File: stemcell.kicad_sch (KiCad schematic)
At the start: 36 parts, among them J1 USB C Connector, J2 Left, J3 Right, J4 Down, SW1 Boot0, U1 STM32F4x1CxUx, U2 XC6220B331MR, Y1 HSE1 8Mhz 12pF

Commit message: updated to use type-c-31-m-12, since it's more commonly available
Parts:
- J1: footprint stemcell:USB-C-C168688 -> Connector_USB:USB_C_Receptacle_HRO_TYPE-C-31-M-12; LCSC C2681554 -> C165948
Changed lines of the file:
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@@
     (property "Reference" "J1" (id 0) (at 123.952 30.734 0))
     (property "Value" "USB C Connector" (id 1) (at 123.952 33.274 0))
-    (property "Footprint" "stemcell:USB-C-C168688" (id 2) (at 127.762 54.229 0)
+    (property "Footprint" "Connector_USB:USB_C_Receptacle_HRO_TYPE-C-31-M-12" (id 2) (at 127.762 54.229 0)
       (effects (font (size 1.27 1.27)) hide)
     )
@@
       (effects (font (size 1.27 1.27)) hide)
     )
-    (property "LCSC" "C2681554" (id 4) (at 123.952 54.229 0)
+    (property "LCSC" "C165948" (id 4) (at 123.952 54.229 0)
       (effects (font (size 1.27 1.27)) hide)
     )
@@
     )
     (path "/a4788c8d-5773-43fe-9711-99f01fa6cfd8"
-      (reference "J1") (unit 1) (value "USB C Connector") (footprint "stemcell:USB-C-C168688")
+      (reference "J1") (unit 1) (value "USB C Connector") (footprint "Connector_USB:USB_C_Receptacle_HRO_TYPE-C-31-M-12")
     )
     (path "/30cde441-a4b4-4a86-92b5-1140e5d06e66"

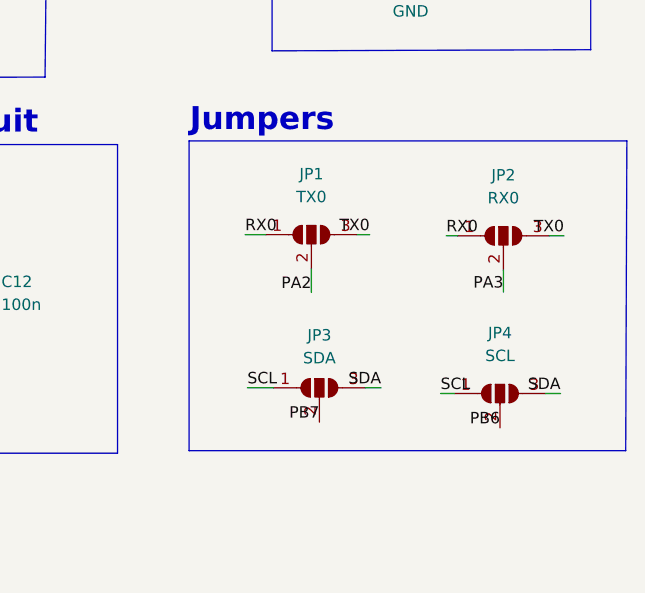
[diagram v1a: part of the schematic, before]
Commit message: added pre-soldered jumpers on the N position, can be cut with razor blade to remove
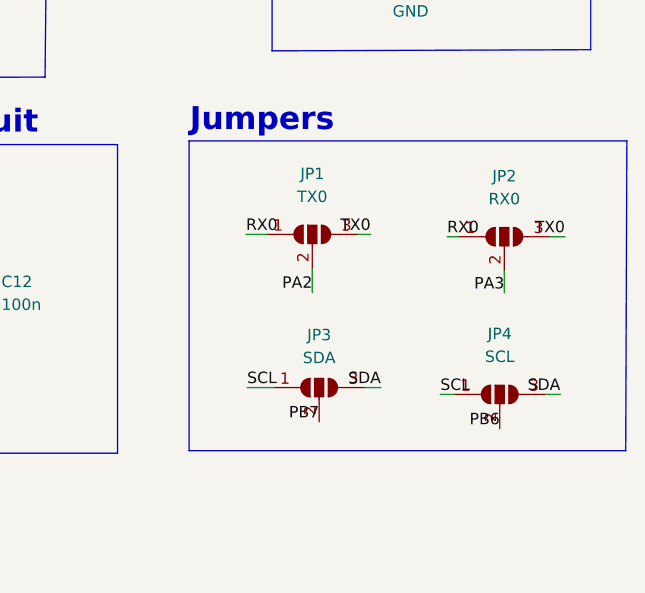
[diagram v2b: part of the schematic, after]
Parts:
- JP1, JP3: footprint stemcell:SOLDER_JUMPER_3 -> stemcell:SOLDER_JUMPER_3_2_3
- JP2, JP4: footprint stemcell:SOLDER_JUMPER_3 -> stemcell:SOLDER_JUMPER_3_1_2
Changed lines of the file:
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@@
     (stroke (width 0) (type default) (color 0 0 0 0))
   )
-  (wire (pts (xy 236.6264 138.9634) (xy 238.9124 138.9634))
+  (wire (pts (xy 236.728 138.938) (xy 239.014 138.938))
     (stroke (width 0) (type default) (color 0 0 0 0))
   )
@@
     (stroke (width 0) (type default) (color 0 0 0 0))
   )
-  (wire (pts (xy 250.4694 138.9634) (xy 249.0724 138.9634))
+  (wire (pts (xy 250.571 138.938) (xy 249.174 138.938))
     (stroke (width 0) (type default) (color 0 0 0 0))
   )
@@
     (stroke (width 0) (type default) (color 0 0 0 0))
   )
-  (wire (pts (xy 271.6784 156.6164) (xy 270.0274 156.6164))
+  (wire (pts (xy 271.653 156.718) (xy 270.002 156.718))
     (stroke (width 0) (type default) (color 0 0 0 0))
   )
@@
     (stroke (width 0) (type default) (color 0 0 0 0))
   )
-  (wire (pts (xy 258.3434 156.6164) (xy 259.8674 156.6164))
+  (wire (pts (xy 258.318 156.718) (xy 259.842 156.718))
     (stroke (width 0) (type default) (color 0 0 0 0))
   )
@@
     (stroke (width 0) (type default) (color 0 0 0 0))
   )
-  (wire (pts (xy 265.3284 145.3388) (xy 265.3284 142.9004))
+  (wire (pts (xy 265.43 145.4404) (xy 265.43 143.002))
     (stroke (width 0) (type default) (color 0 0 0 0))
   )
@@
     (stroke (width 0) (type default) (color 0 0 0 0))
   )
-  (wire (pts (xy 251.7394 155.9814) (xy 249.9614 155.9814))
+  (wire (pts (xy 251.714 155.956) (xy 249.936 155.956))
     (stroke (width 0) (type default) (color 0 0 0 0))
   )
@@
     (stroke (width 0) (type default) (color 0 0 0 0))
   )
-  (wire (pts (xy 236.8804 155.9814) (xy 239.8014 155.9814))
+  (wire (pts (xy 236.855 155.956) (xy 239.776 155.956))
     (stroke (width 0) (type default) (color 0 0 0 0))
   )
@@
     (stroke (width 0) (type default) (color 0 0 0 0))
   )
-  (wire (pts (xy 258.9784 139.0904) (xy 260.2484 139.0904))
+  (wire (pts (xy 259.08 139.192) (xy 260.35 139.192))
     (stroke (width 0) (type default) (color 0 0 0 0))
   )
@@
     (stroke (width 0) (type default) (color 0 0 0 0))
   )
-  (wire (pts (xy 272.0594 139.0904) (xy 270.4084 139.0904))
+  (wire (pts (xy 272.161 139.192) (xy 270.51 139.192))
     (stroke (width 0) (type default) (color 0 0 0 0))
   )
@@
     (stroke (width 0) (type default) (color 0 0 0 0))
   )
-  (wire (pts (xy 243.9924 145.3896) (xy 243.9924 142.7734))
+  (wire (pts (xy 244.094 145.3642) (xy 244.094 142.748))
     (stroke (width 0) (type default) (color 0 0 0 0))
   )
@@
     (effects (font (size 1.27 1.27)) (justify right bottom))
   )
-  (label "SCL" (at 236.8804 155.9814 0)
+  (label "SCL" (at 236.855 155.956 0)
     (effects (font (size 1.27 1.27)) (justify left bottom))
   )
@@
     (effects (font (size 1.27 1.27)) (justify left bottom))
   )
-  (label "SDA" (at 271.6784 156.6164 180)
+  (label "SDA" (at 271.653 156.718 180)
     (effects (font (size 1.27 1.27)) (justify right bottom))
   )
@@
     (effects (font (size 1.27 1.27)) (justify left bottom))
   )
-  (label "SCL" (at 258.3434 156.6164 0)
+  (label "SCL" (at 258.318 156.718 0)
     (effects (font (size 1.27 1.27)) (justify left bottom))
   )
@@
     (effects (font (size 1.27 1.27)) (justify right bottom))
   )
-  (label "PA2" (at 243.9924 145.3896 180)
+  (label "PA2" (at 244.094 145.3642 180)
     (effects (font (size 1.27 1.27)) (justify right bottom))
   )
@@
     (effects (font (size 1.27 1.27)) (justify left bottom))
   )
-  (label "TX0" (at 250.4694 138.9634 180)
+  (label "TX0" (at 250.571 138.938 180)
     (effects (font (size 1.27 1.27)) (justify right bottom))
   )
@@
     (effects (font (size 1.27 1.27)) (justify right bottom))
   )
-  (label "PB7" (at 244.8814 159.7914 180)
+  (label "PB7" (at 244.856 159.766 180)
     (effects (font (size 1.27 1.27)) (justify right bottom))
   )
@@
     (effects (font (size 1.27 1.27)) (justify left bottom))
   )
-  (label "SDA" (at 251.7394 155.9814 180)
+  (label "SDA" (at 251.714 155.956 180)
     (effects (font (size 1.27 1.27)) (justify right bottom))
   )
@@
     (effects (font (size 1.27 1.27)) (justify right bottom))
   )
-  (label "PA3" (at 265.3284 145.3388 180)
+  (label "PA3" (at 265.43 145.4404 180)
     (effects (font (size 1.27 1.27)) (justify right bottom))
   )
@@
     (effects (font (size 1.27 1.27)) (justify left bottom))
   )
-  (label "RX0" (at 236.6264 138.9634 0)
+  (label "RX0" (at 236.728 138.938 0)
     (effects (font (size 1.27 1.27)) (justify left bottom))
   )
@@
     (effects (font (size 1.27 1.27)) (justify right bottom))
   )
-  (label "PB6" (at 264.9474 160.4264 180)
+  (label "PB6" (at 264.922 160.528 180)
     (effects (font (size 1.27 1.27)) (justify right bottom))
   )
@@
     (effects (font (size 1.27 1.27)) (justify left bottom))
   )
-  (label "RX0" (at 258.9784 139.0904 0)
+  (label "RX0" (at 259.08 139.192 0)
     (effects (font (size 1.27 1.27)) (justify left bottom))
   )
@@
     (effects (font (size 1.27 1.27)) (justify left bottom))
   )
-  (label "TX0" (at 272.0594 139.0904 180)
+  (label "TX0" (at 272.161 139.192 180)
     (effects (font (size 1.27 1.27)) (justify right bottom))
   )
@@
     (pin "2")
   )
-  (symbol (lib_id "Jumper:SolderJumper_3_Open") (at 243.9924 138.9634 0) (unit 1)
-    (in_bom yes) (on_board yes) (fields_autoplaced)
-    (property "Reference" "JP1" (id 0) (at 243.9924 132.2324 0))
-    (property "Value" "TX0" (id 1) (at 243.9924 134.7724 0))
-    (property "Footprint" "stemcell:SOLDER_JUMPER_3" (id 2) (at 243.9924 138.9634 0)
-      (effects (font (size 1.27 1.27)) hide)
-    )
-    (property "Datasheet" "~" (id 3) (at 243.9924 138.9634 0)
+  (symbol (lib_id "Jumper:SolderJumper_3_Open") (at 244.094 138.938 0) (unit 1)
+    (in_bom yes) (on_board yes) (fields_autoplaced)
+    (property "Reference" "JP1" (id 0) (at 244.094 132.207 0))
+    (property "Value" "TX0" (id 1) (at 244.094 134.747 0))
+    (property "Footprint" "stemcell:SOLDER_JUMPER_3_2_3" (id 2) (at 244.094 138.938 0)
+      (effects (font (size 1.27 1.27)) hide)
+    )
+    (property "Datasheet" "~" (id 3) (at 244.094 138.938 0)
       (effects (font (size 1.27 1.27)) hide)
     )
@@
     (pin "2")
   )
-  (symbol (lib_id "Jumper:SolderJumper_3_Open") (at 265.3284 139.0904 0) (unit 1)
-    (in_bom yes) (on_board yes) (fields_autoplaced)
-    (property "Reference" "JP2" (id 0) (at 265.3284 132.3594 0))
-    (property "Value" "RX0" (id 1) (at 265.3284 134.8994 0))
-    (property "Footprint" "stemcell:SOLDER_JUMPER_3" (id 2) (at 265.3284 139.0904 0)
-      (effects (font (size 1.27 1.27)) hide)
-    )
-    (property "Datasheet" "~" (id 3) (at 265.3284 139.0904 0)
+  (symbol (lib_id "Jumper:SolderJumper_3_Open") (at 265.43 139.192 0) (unit 1)
+    (in_bom yes) (on_board yes) (fields_autoplaced)
+    (property "Reference" "JP2" (id 0) (at 265.43 132.461 0))
+    (property "Value" "RX0" (id 1) (at 265.43 135.001 0))
+    (property "Footprint" "stemcell:SOLDER_JUMPER_3_1_2" (id 2) (at 265.43 139.192 0)
+      (effects (font (size 1.27 1.27)) hide)
+    )
+    (property "Datasheet" "~" (id 3) (at 265.43 139.192 0)
       (effects (font (size 1.27 1.27)) hide)
     )
@@
     (pin "1")
   )
-  (symbol (lib_id "Jumper:SolderJumper_3_Open") (at 264.9474 156.6164 0) (unit 1)
-    (in_bom yes) (on_board yes)
-    (property "Reference" "JP4" (id 0) (at 264.9474 149.8854 0))
-    (property "Value" "SCL" (id 1) (at 264.9474 152.4254 0))
-    (property "Footprint" "stemcell:SOLDER_JUMPER_3" (id 2) (at 264.9474 156.6164 0)
-      (effects (font (size 1.27 1.27)) hide)
-    )
-    (property "Datasheet" "~" (id 3) (at 264.9474 156.6164 0)
+  (symbol (lib_id "Jumper:SolderJumper_3_Open") (at 264.922 156.718 0) (unit 1)
+    (in_bom yes) (on_board yes)
+    (property "Reference" "JP4" (id 0) (at 264.922 149.987 0))
+    (property "Value" "SCL" (id 1) (at 264.922 152.527 0))
+    (property "Footprint" "stemcell:SOLDER_JUMPER_3_1_2" (id 2) (at 264.922 156.718 0)
+      (effects (font (size 1.27 1.27)) hide)
+    )
+    (property "Datasheet" "~" (id 3) (at 264.922 156.718 0)
       (effects (font (size 1.27 1.27)) hide)
     )
@@
     (pin "2")
   )
-  (symbol (lib_id "Jumper:SolderJumper_3_Open") (at 244.8814 155.9814 0) (unit 1)
-    (in_bom yes) (on_board yes) (fields_autoplaced)
-    (property "Reference" "JP3" (id 0) (at 244.8814 150.1394 0))
-    (property "Value" "SDA" (id 1) (at 244.8814 152.6794 0))
-    (property "Footprint" "stemcell:SOLDER_JUMPER_3" (id 2) (at 244.8814 155.9814 0)
-      (effects (font (size 1.27 1.27)) hide)
-    )
-    (property "Datasheet" "~" (id 3) (at 244.8814 155.9814 0)
+  (symbol (lib_id "Jumper:SolderJumper_3_Open") (at 244.856 155.956 0) (unit 1)
+    (in_bom yes) (on_board yes) (fields_autoplaced)
+    (property "Reference" "JP3" (id 0) (at 244.856 150.114 0))
+    (property "Value" "SDA" (id 1) (at 244.856 152.654 0))
+    (property "Footprint" "stemcell:SOLDER_JUMPER_3_2_3" (id 2) (at 244.856 155.956 0)
+      (effects (font (size 1.27 1.27)) hide)
+    )
+    (property "Datasheet" "~" (id 3) (at 244.856 155.956 0)
       (effects (font (size 1.27 1.27)) hide)
     )
@@
     )
     (path "/3b6d7996-cb03-421c-89b7-14690c1f4b89"
-      (reference "JP1") (unit 1) (value "TX0") (footprint "stemcell:SOLDER_JUMPER_3")
+      (reference "JP1") (unit 1) (value "TX0") (footprint "stemcell:SOLDER_JUMPER_3_2_3")
     )
     (path "/5e4a462a-cd9e-453d-8ddc-65f701dafe84"
-      (reference "JP2") (unit 1) (value "RX0") (footprint "stemcell:SOLDER_JUMPER_3")
+      (reference "JP2") (unit 1) (value "RX0") (footprint "stemcell:SOLDER_JUMPER_3_1_2")
     )
     (path "/e1ed2867-9986-47bf-b812-c7fb4588f3c6"
-      (reference "JP3") (unit 1) (value "SDA") (footprint "stemcell:SOLDER_JUMPER_3")
+      (reference "JP3") (unit 1) (value "SDA") (footprint "stemcell:SOLDER_JUMPER_3_2_3")
     )
     (path "/ad93f2ec-4e50-43bd-9256-b09b41c0ee99"
-      (reference "JP4") (unit 1) (value "SCL") (footprint "stemcell:SOLDER_JUMPER_3")
+      (reference "JP4") (unit 1) (value "SCL") (footprint "stemcell:SOLDER_JUMPER_3_1_2")
     )
     (path "/ee45be93-fd9f-4d18-97ee-e75a85927397"
